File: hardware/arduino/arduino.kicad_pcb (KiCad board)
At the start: 2 copper layers, 160 x 100 mm, 14 parts, among them J1 Conn_01x08_Male, J2 Conn_01x08_Male, J3 Conn_01x08_Male, J4 Conn_01x08_Male, J5 Conn_01x08_Male, J6 Conn_01x10_Male, J7 Conn_02x18_Odd_Even, SW1 SW_Push

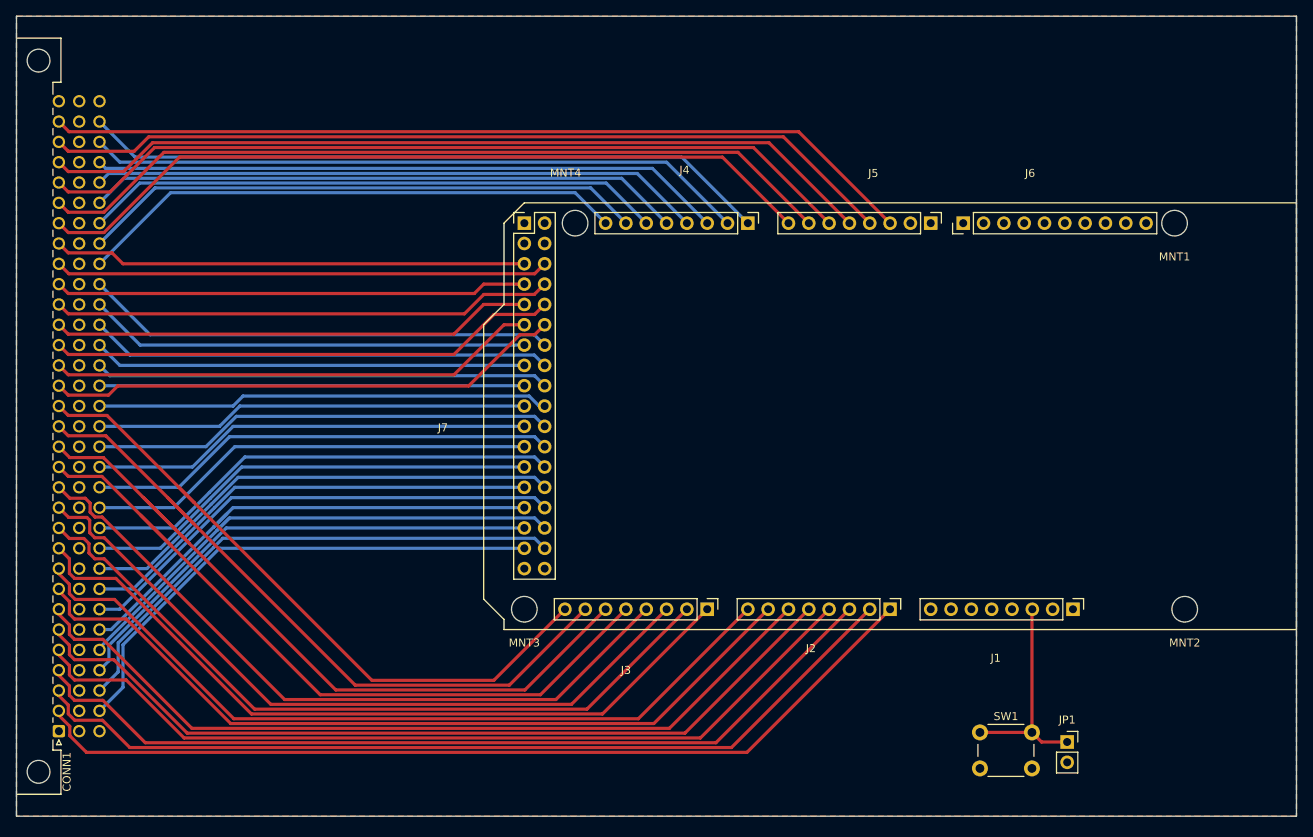
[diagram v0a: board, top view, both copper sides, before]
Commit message: arduino: add more headers and annotations
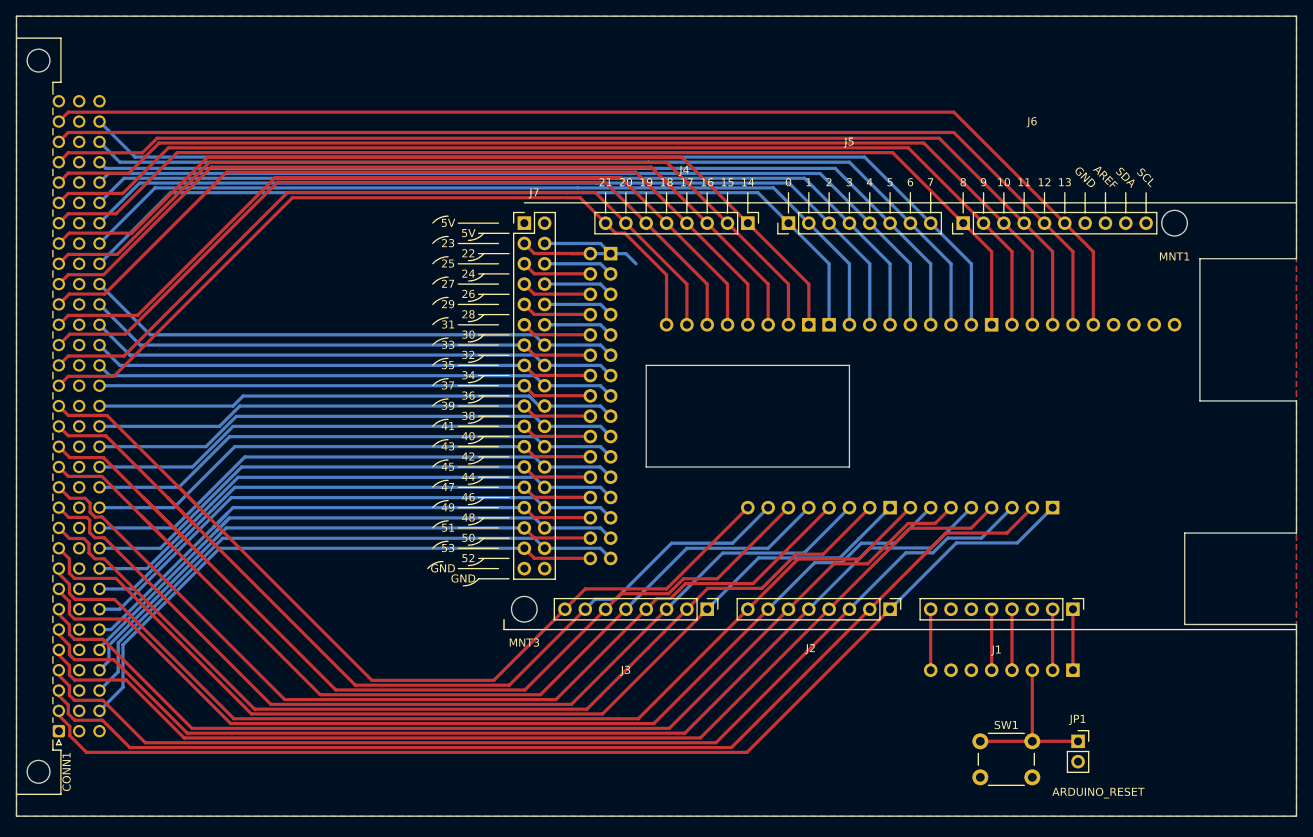
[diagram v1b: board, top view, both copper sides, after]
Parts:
- removed MNT2, MNT4: MountingHole_3.2mm_M3, MountingHole:MountingHole_3.2mm_M3
- added J10: Conn_01x08_Male, Connector_PinHeader_2.54mm:PinHeader_1x08_P2.54mm_Vertical, B.Cu at (185.2, 104.2)
- added J11: Conn_01x08_Male, Connector_PinHeader_2.54mm:PinHeader_1x08_P2.54mm_Vertical, B.Cu at (164.8, 104.2)
- added J12: Conn_01x08_Male, Connector_PinHeader_2.54mm:PinHeader_1x08_P2.54mm_Vertical, B.Cu at (157.2, 81.3)
- added J13: Conn_01x08_Male, Connector_PinHeader_2.54mm:PinHeader_1x08_P2.54mm_Vertical, B.Cu at (187.7, 124.5)
- added J14: Conn_02x16_Odd_Even, Connector_PinHeader_2.54mm:PinHeader_2x16_P2.54mm_Vertical, B.Cu at (129.9, 72.4)
- added J8: Conn_01x10_Male, Connector_PinHeader_2.54mm:PinHeader_1x10_P2.54mm_Vertical, B.Cu at (177.5, 81.3)
- added J9: Conn_01x08_Male, Connector_PinHeader_2.54mm:PinHeader_1x08_P2.54mm_Vertical, B.Cu at (154.7, 81.3)
- moved J5 17.8 mm to (152.1, 68.6), turned to 90 degrees
- moved JP1 1.36 mm to (188.3, 133.4)
- moved SW1 1.12 mm to (176.1, 133.4)
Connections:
- net /a0 renamed 54
- net /a1 renamed 55
- net /a10 renamed 64
- net /a11 renamed 65
- net /a12 renamed 69
- net /a13 renamed 68
- net /a14 renamed 67
- net /a15 renamed 66
- net /a2 renamed 56
- net /a3 renamed 57
- net /a4 renamed 58
- net /a5 renamed 59
- net /a6 renamed 60
- net /a7 renamed 61
- net /a8 renamed 62
- net /a9 renamed 63
- net /pa0 renamed 51
- net /pa1 renamed 50
- net /pa2 renamed 49
- net /pa3 renamed 48
- net /pa4 renamed 47
- net /pa5 renamed 46
- net /pa6 renamed 45
- net /pa7 renamed 44
- net /pb0 renamed 43
- net /pb1 renamed 42
- net /pb2 renamed 41
- net /pb3 renamed 40
- net /pb4 renamed 39
- net /pb5 renamed 38
- net /pb6 renamed 37
- net /pb7 renamed 36
- net CA1 renamed 53
- net CA2 renamed 52
- net CB1 renamed 35
- net CB2 renamed 34
- net Net-(J1-Pad3) renamed A_RESET
- net ~MP_RST~ renamed 33
- net ~RST~ renamed 32
- CONN1 pad A18: /d7 -> 21
- CONN1 pad A19: /d6 -> 20
- CONN1 pad A20: /d5 -> 19
- CONN1 pad A21: /d4 -> 18
- CONN1 pad A22: /d3 -> 17
- CONN1 pad A23: /d2 -> 16
- CONN1 pad A24: /d1 -> 15
- CONN1 pad A25: /d0 -> 14
- CONN1 pad A26: RDY -> 8
- CONN1 pad A27: ~BUS_ACTIVE~ -> 9
- CONN1 pad A28: SYS_CLK -> 10
- CONN1 pad A29: ~S_BUS~ -> 11
- CONN1 pad A30: ~NMI~ -> 12
- CONN1 pad A31: BUS_CLK -> 13
- CONN1 pad C24: /bd5 -> 0
- CONN1 pad C25: /bd4 -> 1
- CONN1 pad C26: /bd3 -> 2
- CONN1 pad C27: /bd2 -> 3
- CONN1 pad C28: /bd1 -> 4
- CONN1 pad C29: /bd0 -> 5
- CONN1 pad C30: R~W~ -> 6
- CONN1 pad C31: ~RST_HDR~ -> 7
- J1 pad 1: Net-(J1-Pad1) -> NC
- J1 pad 2: Net-(J1-Pad2) -> IOREF
- J1 pad 4: Net-(J1-Pad4) -> A_3V3
- J1 pad 5: Net-(J1-Pad5) -> A_5V
- J1 pad 8: Net-(J1-Pad8) -> A_VIN
- J4 pad 1: ~RST_HDR~ -> 14
- J4 pad 2: R~W~ -> 15
- J4 pad 3: /bd0 -> 16
- J4 pad 4: /bd1 -> 17
- J4 pad 5: /bd2 -> 18
- J4 pad 6: /bd3 -> 19
- J4 pad 7: /bd4 -> 20
- J4 pad 8: /bd5 -> 21
- J5 pad 1: Net-(J5-Pad1) -> 0
- J5 pad 2: Net-(J5-Pad2) -> 1
- J5 pad 3: BUS_CLK -> 2
- J5 pad 4: ~NMI~ -> 3
- J5 pad 5: ~S_BUS~ -> 4
- J5 pad 6: SYS_CLK -> 5
- J5 pad 7: ~BUS_ACTIVE~ -> 6
- J5 pad 8: RDY -> 7
- J6 pad 1: Net-(J6-Pad1) -> 8
- J6 pad 2: Net-(J6-Pad2) -> 9
- J6 pad 3: Net-(J6-Pad3) -> 10
- J6 pad 4: Net-(J6-Pad4) -> 11
- J6 pad 5: Net-(J6-Pad5) -> 12
- J6 pad 6: Net-(J6-Pad6) -> 13
- J7 pad 10: /d5 -> 28
- J7 pad 11: /d6 -> 31
- J7 pad 12: /d7 -> 30
- J7 pad 3: Net-(J7-Pad3) -> 23
- J7 pad 4: Net-(J7-Pad4) -> 22
- J7 pad 5: /d0 -> 25
- J7 pad 6: /d1 -> 24
- J7 pad 7: /d2 -> 27
- J7 pad 8: /d3 -> 26
- J7 pad 9: /d4 -> 29
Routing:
- net 13: track 0.00 -> 146.2 mm
- net 12: track 0.00 -> 142.6 mm
- net 11: track 0.00 -> 140.5 mm
- net 10: track 0.00 -> 138.5 mm
- net 9: track 0.00 -> 136.5 mm
- net 8: track 0.00 -> 134.5 mm
- net 7: track 0.00 -> 124.0 mm
- net 6: track 0.00 -> 120.4 mm
- net 5: track 0.00 -> 116.8 mm
- net 4: track 0.00 -> 114.1 mm
- net 3: track 0.00 -> 112.1 mm
- net 2: track 0.00 -> 110.2 mm
- net 14: track 0.00 -> 109.8 mm
- net BUS_CLK: track 109.2 -> 0.00 mm
- net 1: track 0.00 -> 108.2 mm
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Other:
- outline, holes or cut-outs redrawn
- board text added: "0"
- board text added: "1"
- board text added: "10"
- board text added: "11"
- board text added: "12"
- board text added: "13"
- board text added: "14"
- board text added: "15"
- board text added: "16"
- board text added: "17"
- board text added: "18"
- board text added: "19"
- board text added: "2"
- board text added: "20"
- board text added: "21"
- board text added: "22"
- board text added: "23"
- board text added: "24"
- board text added: "25"
- board text added: "26"
- board text added: "27"
- board text added: "28"
- board text added: "29"
- board text added: "3"
- board text added: "30"
- board text added: "31"
- board text added: "32"
- board text added: "33"
- board text added: "34"
- board text added: "35"
- board text added: "36"
- board text added: "37"
- board text added: "38"
- board text added: "39"
- board text added: "3V3"
- board text added: "4"
- board text added: "40"
- board text added: "41"
- board text added: "42"
- board text added: "43"
- board text added: "44"
- board text added: "45"
- board text added: "46"
- board text added: "47"
- board text added: "48"
- board text added: "49"
- board text added: "5"
- board text added: "50"
- board text added: "51"
- board text added: "52"
- board text added: "53"
- board text added: "54"
- board text added: "55"
- board text added: "56"
- board text added: "57"
- board text added: "58"
- board text added: "59"
- board text added: "5V"
- board text added: "6"
- board text added: "60"
- board text added: "61"
- board text added: "62"
- board text added: "63"
- board text added: "64"
- board text added: "65"
- board text added: "66"
- board text added: "67"
- board text added: "68"
- board text added: "69"
- board text added: "7"
- board text added: "8"
- board text added: "9"
- board text added: "ARDUINO_RESET"
- board text added: "AREF"
- board text added: "A_RST"
- board text added: "A_VIN"
- board text added: "GND"
- board text added: "IOREF"
- board text added: "NC"
- board text added: "SCL"
- board text added: "SDA"

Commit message: arduino: add annotations and some pins
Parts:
- added G***: LOGO, graphics:qr_code, F.Cu at (159.1, 135.3)
- added G***: LOGO, graphics:microclem_logo_mask, F.Cu at (205.5, 52.1)
- added J15: Conn_01x01_Male, Connector_PinHeader_2.54mm:PinHeader_1x01_P2.54mm_Vertical, F.Cu at (120.6, 137.7)
- added J16: Conn_01x01_Male, Connector_PinHeader_2.54mm:PinHeader_1x01_P2.54mm_Vertical, F.Cu at (120.6, 48.3)
- added J17: Conn_01x01_Male, Connector_PinHeader_2.54mm:PinHeader_1x01_P2.54mm_Vertical, B.Cu at (125.7, 137.7)
- added J18: Conn_01x01_Male, Connector_PinHeader_2.54mm:PinHeader_1x01_P2.54mm_Vertical, B.Cu at (125.7, 48.3)
- added REF**: OSHW-Logo_11.4x12mm_SilkScreen, Symbol:OSHW-Logo_11.4x12mm_SilkScreen, F.Cu at (202.9, 133.4)
- JP1: footprint Connector_PinSocket_2.54mm:PinSocket_1x02_P2.54mm_Vertical -> Connector_PinHeader_2.54mm:PinHeader_1x02_P2.54mm_Vertical
- moved JP1 18.5 mm to (169.9, 135.3)
- moved SW1 1.91 mm to (176.1, 135.3)
- moved J13 1.27 mm to (187.7, 125.8)
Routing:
- net A_RESET: track 21.2 -> 31.2 mm
- net (no net): track 8.78 -> 0.00 mm
- net NC: track 7.62 -> 8.89 mm
- net IOREF: track 7.62 -> 8.89 mm
- net A_VIN: track 7.62 -> 8.89 mm
- net A_5V: track 7.62 -> 8.89 mm
- net A_3V3: track 7.62 -> 8.89 mm
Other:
- outline, holes or cut-outs redrawn
- board text added: "0 1 2 3 4 5 6 7 8 9 10 11 12 13 14 15 16 17 18 19 20 21 22 23 24 25 26 27 28 29 30 31"
- board text added: "32 33 34 35 36 37 38 39 40 41 42 43 44 45 46 47 48 49 50 51 52 53 54 55 56 57 58 59 60 61 62 63 64 65 66 67 68 69"
- board text added: "A"
- board text added: "Arduino microclem monitor Alex Ford 2021-03-13 microclem.com"
- board text added: "B"
- board text added: "C"
- board text added: "For Arduino Mega 2560"
- board text added: "bd5 bd4 bd3 bd2 bd1 bd0 R~W~ ~RST_HDR~ RDY ~BUS_ACTIVE~ SYS_CLK ~S_BUS~ ~NMI~ BUS_CLK d0 d1 d2 d3 d4 d5 d6 d7 - - - - - - - - - -"
- board text added: "~RST~ ~MP_RST~ CB2 CB1 pb7 pb6 pb5 pb4 pb3 pb2 pb1 pb0 pa7 pa6 pa5 pa4 pa3 pa2 pa1 pa0 CA2 CA1 a0 a1 a2 a3 a4 a5 a6 a7 a8 a9 a10 a11 a12 a13 a14 a15"

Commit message: arduino: minor tweaks
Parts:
- J15, J18: value Conn_01x01_Male -> Conn_02x02_Odd_Even; footprint Connector_PinHeader_2.54mm:PinHeader_1x01_P2.54mm_Vertical -> Connector_PinHeader_2.54mm:PinHeader_1x04_P2.54mm_Vertical
- J16: value Conn_01x01_Male -> Conn_02x02_Odd_Even; footprint Connector_PinHeader_2.54mm:PinHeader_1x01_P2.54mm_Vertical -> Connector_PinHeader_2.54mm:PinHeader_1x04_P2.54mm_Vertical; moved to B.Cu
- J17: value Conn_01x01_Male -> Conn_02x02_Odd_Even; footprint Connector_PinHeader_2.54mm:PinHeader_1x01_P2.54mm_Vertical -> Connector_PinHeader_2.54mm:PinHeader_1x04_P2.54mm_Vertical; moved to F.Cu
- moved J17 90.0 mm to (125.6, 47.7), turned to 270 degrees
- moved J16 89.8 mm to (128.1, 137.7), turned to 270 degrees
- moved J18 4.95 mm to (130.6, 47.7), turned to 270 degrees
- moved J15 2.50 mm to (123.1, 137.7), turned to 270 degrees
- moved G*** 0.60 mm to (205.7, 52.6)
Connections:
- J16 pad 1: GND -> +5V
- J17 pad 1: +5V -> GND
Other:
- board text added: "Arduino microclem monitor Alex Ford 2021-03-13 microclem.com [SHA_HERE]"
- board text removed: "Arduino microclem monitor Alex Ford 2021-03-13 microclem.com"
